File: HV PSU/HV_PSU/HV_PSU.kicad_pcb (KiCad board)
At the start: 2 copper layers, 200 x 80 mm, 106 parts, among them J1 Screw_Terminal_01x07, J13 MountingHole_Pad, J2 AC_HV_1, J3 AC_HV_2, J4 MountingHole_Pad, J5 AC_HV_2, J6 MountingHole_Pad, Q1 2N7002, Q2 IRFS4227, Q3 IRFS4227, T1 UY12, U1 L7812, U2 TPS2814D

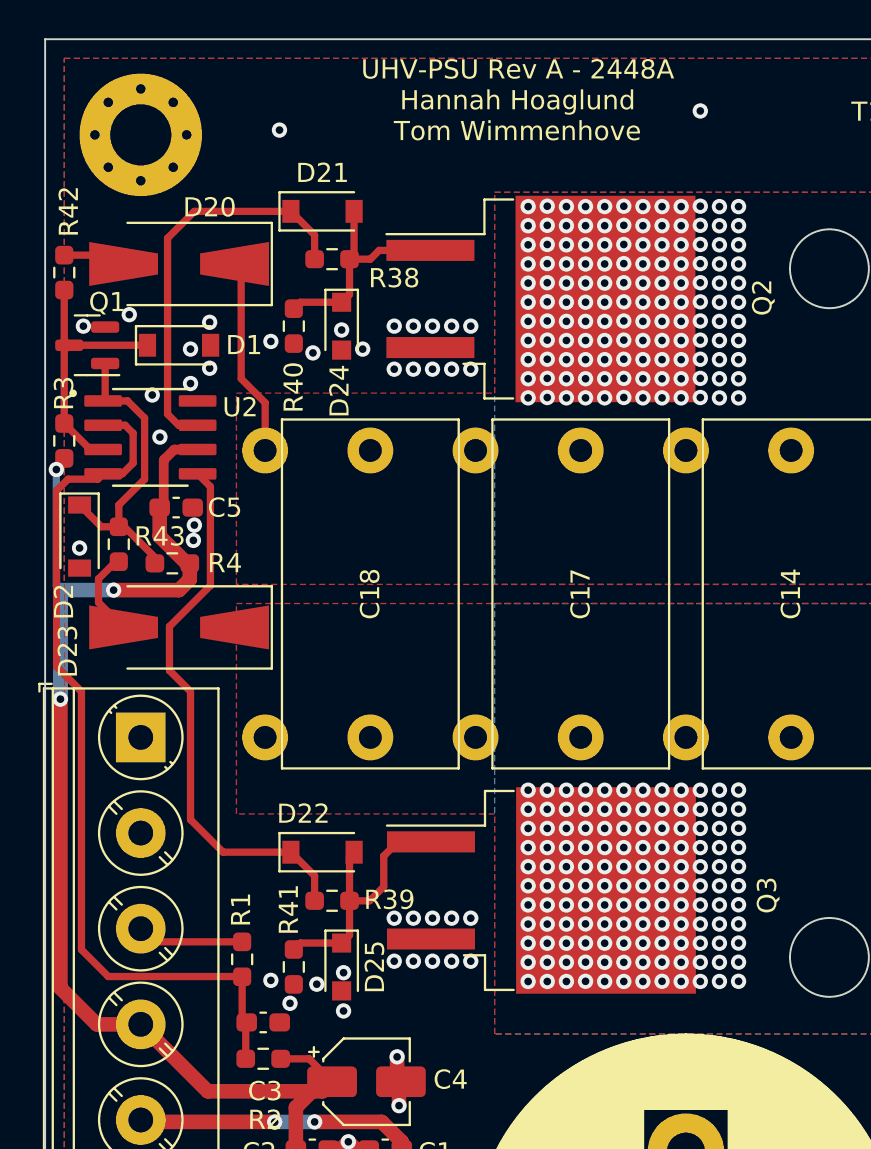
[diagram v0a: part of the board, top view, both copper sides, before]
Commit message: More better ground, planes and thermal reliefs
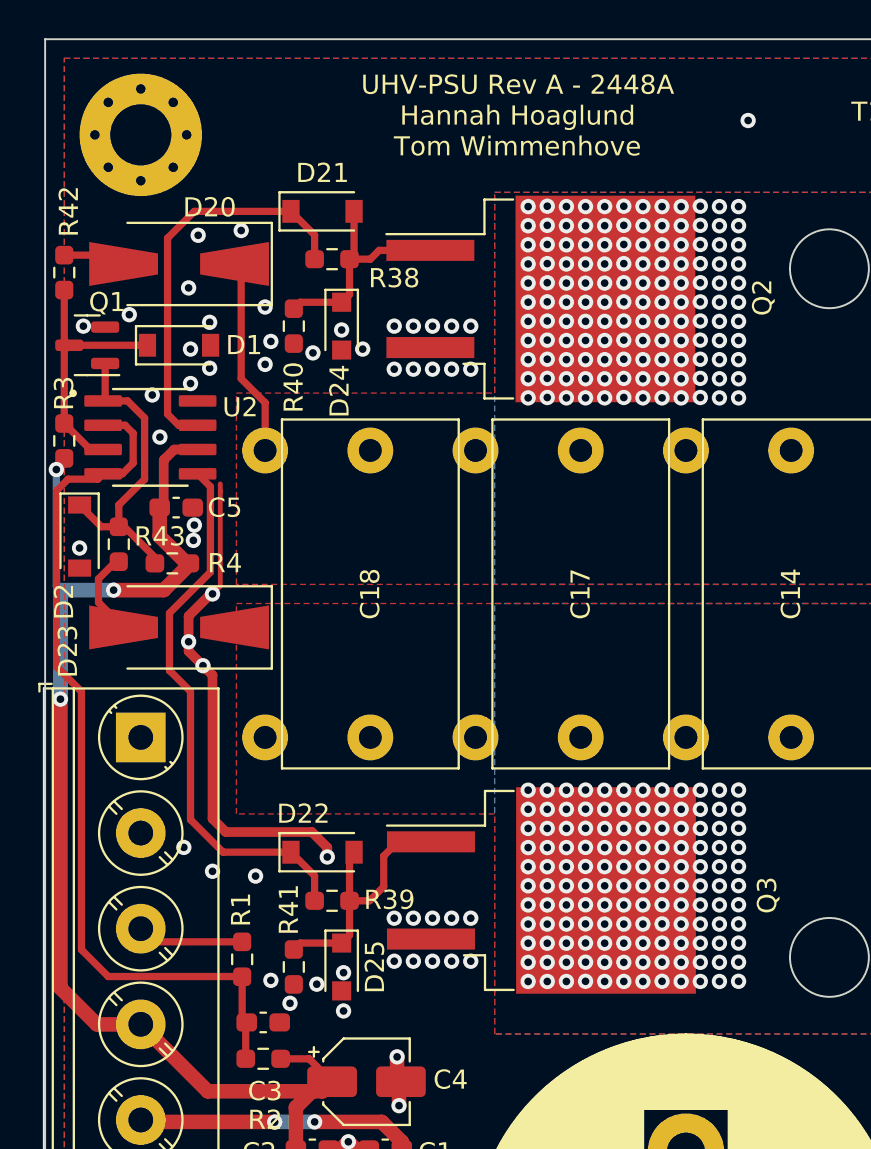
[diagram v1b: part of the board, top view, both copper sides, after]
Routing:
- net GND: track 15.7 -> 41.6 mm, vias 57 -> 68

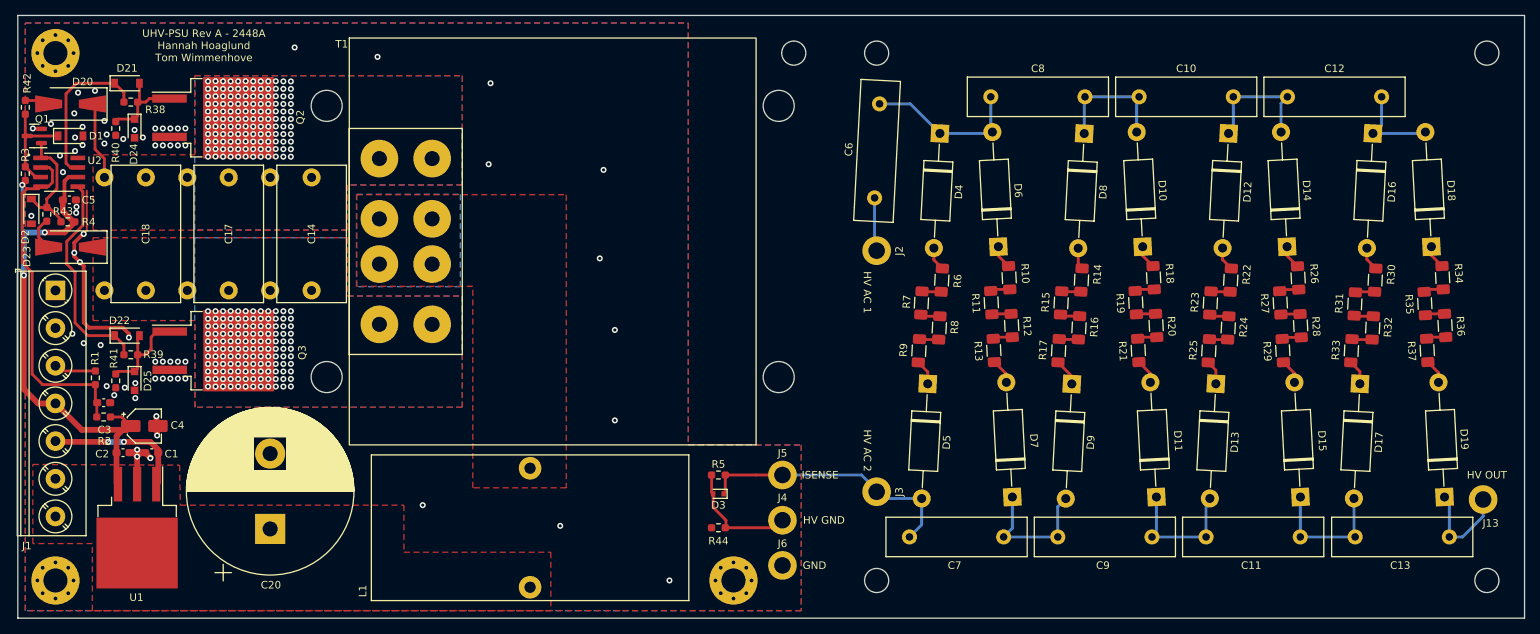
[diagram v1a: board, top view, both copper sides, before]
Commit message: More robust current sense
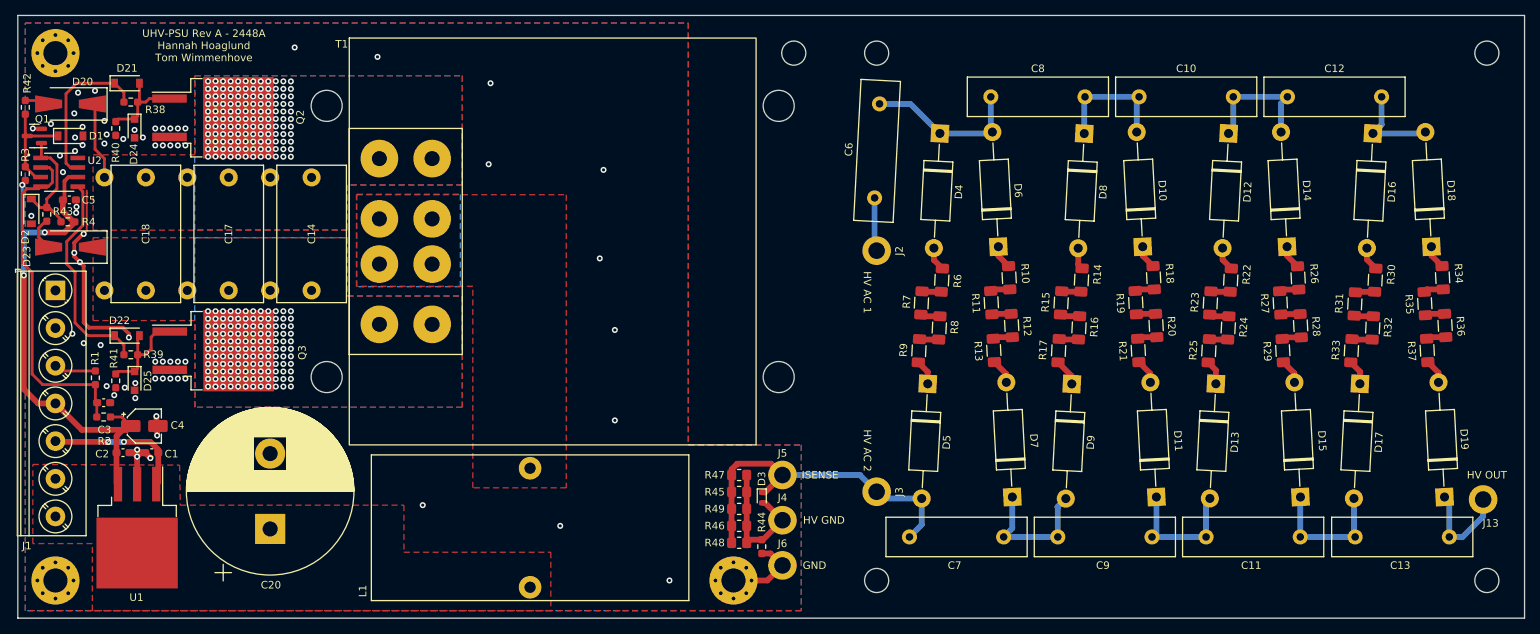
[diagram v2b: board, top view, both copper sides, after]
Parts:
- removed R5: 100, Resistor_SMD:R_0603_1608Metric_Pad0.98x0.95mm_HandSolder
- added R45: 1k, Resistor_SMD:R_0805_2012Metric_Pad1.20x1.40mm_HandSolder, F.Cu at (171.0, 141.5)
- added R46: 1k, Resistor_SMD:R_0805_2012Metric_Pad1.20x1.40mm_HandSolder, F.Cu at (171.0, 146.0)
- added R47: 1k, Resistor_SMD:R_0805_2012Metric_Pad1.20x1.40mm_HandSolder, F.Cu at (171.0, 139.2)
- added R48: 1k, Resistor_SMD:R_0805_2012Metric_Pad1.20x1.40mm_HandSolder, F.Cu at (171.0, 148.2)
- added R49: 1k, Resistor_SMD:R_0805_2012Metric_Pad1.20x1.40mm_HandSolder, F.Cu at (171.0, 143.8)
- moved R44 6.27 mm to (174.0, 148.8), turned to -90 degrees
- moved D3 5.77 mm to (174.0, 142.2), turned to -90 degrees
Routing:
- net Net-(R46-Pad2): track 35.9 -> 46.9 mm
- net GND: track 41.6 -> 52.4 mm
- net GND1: track 15.8 -> 20.1 mm

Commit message: Logos and symbols
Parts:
- added REF**: KiCad-Logo2_5mm_SilkScreen, Symbol:KiCad-Logo2_5mm_SilkScreen, F.Cu at (177.5, 108.5)
- added REF**: OSHW-Logo2_7.3x6mm_SilkScreen, Symbol:OSHW-Logo2_7.3x6mm_SilkScreen, F.Cu at (113.0, 82.2)
- added REF**: Symbol_HighVoltage_Type2_VerySmall, Logo:Symbol_HighVoltage_Type2_VerySmall, F.Cu at (182.5, 120.0)
- added REF**: Symbol_HighVoltage_Type2_VerySmall, Logo:Symbol_HighVoltage_Type2_VerySmall, F.Cu at (269.8, 126.7)
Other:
- board text added: "For negative output, reverse diode polarities"

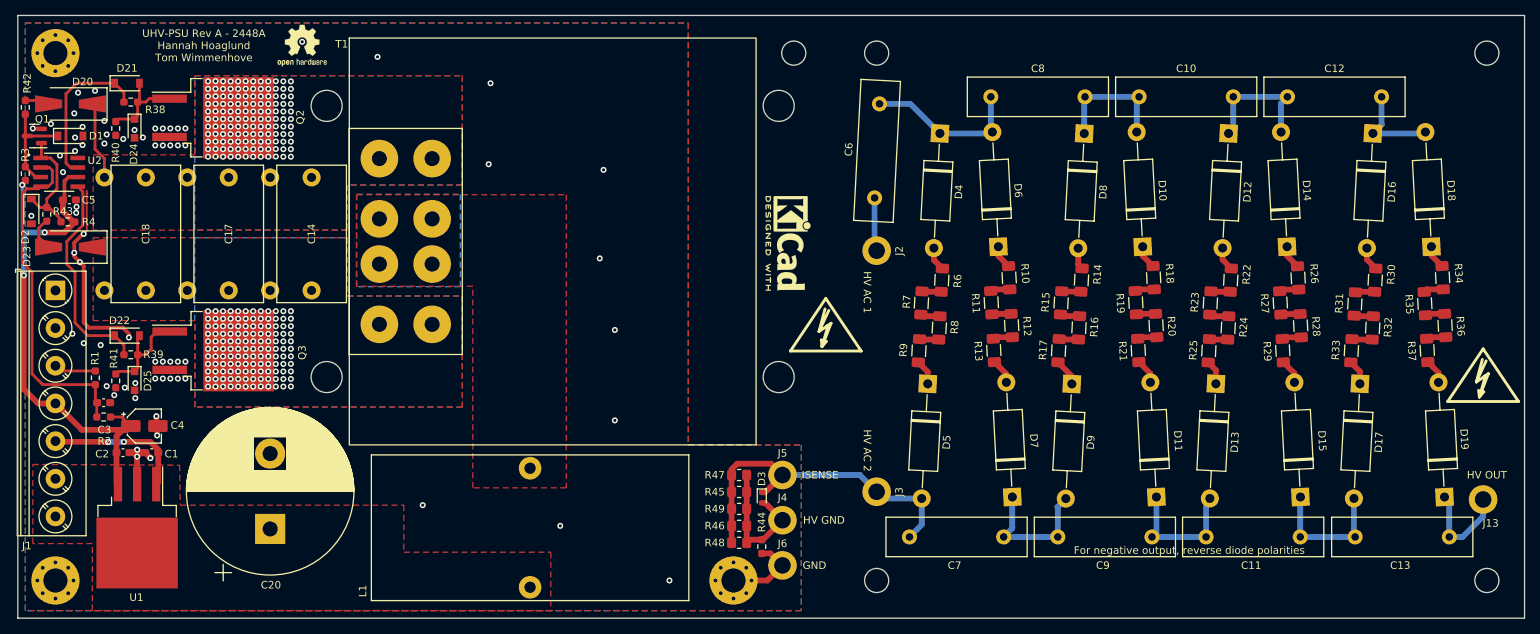
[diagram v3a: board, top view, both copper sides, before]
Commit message: Fixed enable circuit
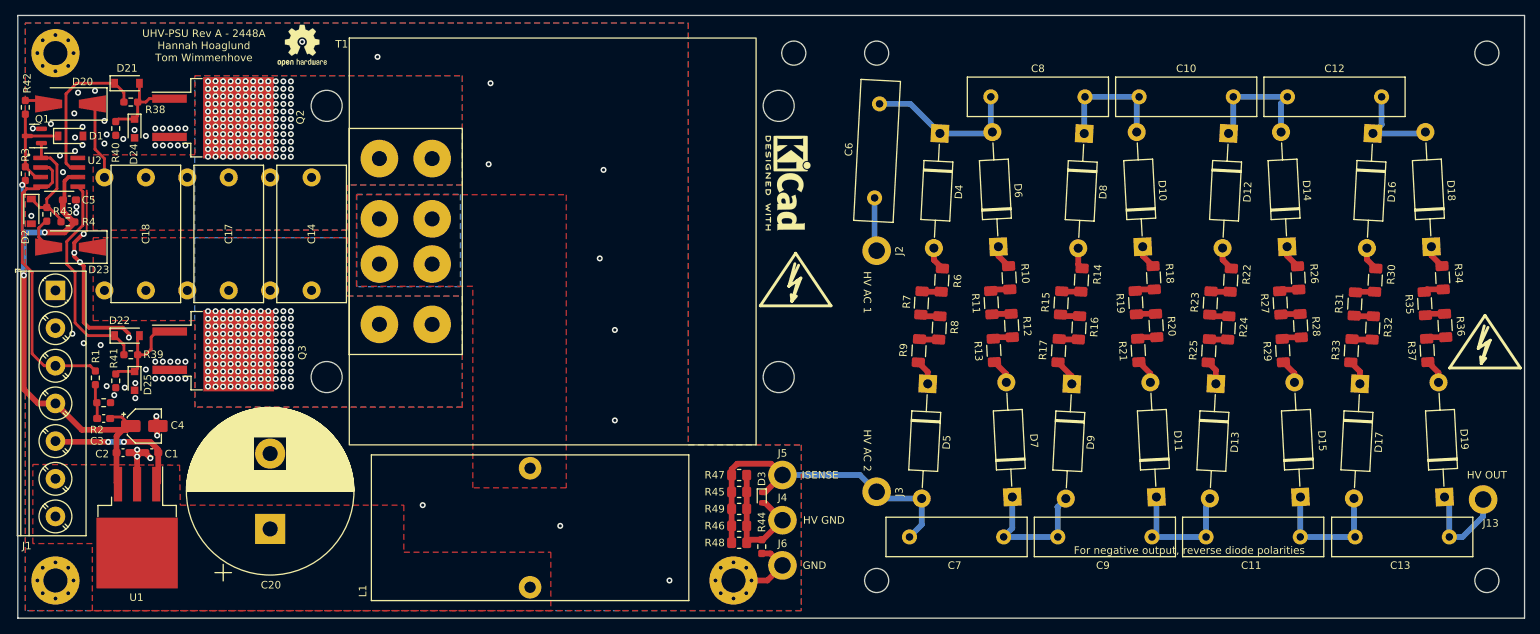
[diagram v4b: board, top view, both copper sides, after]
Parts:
- removed the REF** at (182.5, 120.0)
- removed the REF** at (269.8, 126.7)
- added REF**: Symbol_HighVoltage_Type2_VerySmall, Logo:Symbol_HighVoltage_Type2_VerySmall, F.Cu at (178.5, 114.0)
- added REF**: Symbol_HighVoltage_Type2_VerySmall, Logo:Symbol_HighVoltage_Type2_VerySmall, F.Cu at (270.0, 122.2)
- moved REF** 8.00 mm to (177.5, 100.5)
- moved C3 2.10 mm to (86.7, 131.8), turned to 180 degrees
- moved R2 1.90 mm to (86.7, 129.7), turned to 180 degrees
- turned R1 to -90 degrees
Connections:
- C3 pad 1: Net-(C3-Pad1) -> +12V
- C3 pad 2: GND -> Net-(C3-Pad2)
- R1 pad 1: Net-(C3-Pad1) -> Net-(J1-Pad3)
- R1 pad 2: Net-(J1-Pad3) -> Net-(C3-Pad2)
- R2 pad 1: Net-(C3-Pad1) -> GND
- R2 pad 2: +12V -> Net-(C3-Pad2)
- U2 pad 2: Net-(C3-Pad1) -> Net-(J1-Pad3)
- U2 pad 4: Net-(C3-Pad1) -> Net-(J1-Pad3)
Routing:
- net Net-(C3-Pad1): track 46.0 -> 0.00 mm
- net Net-(J1-Pad3): track 5.71 -> 40.2 mm
- net Net-(C3-Pad2): track 0.00 -> 4.60 mm
- net GND: vias 68 -> 69
